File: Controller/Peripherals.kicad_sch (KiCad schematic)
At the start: 3 parts, among them U601 THB001P

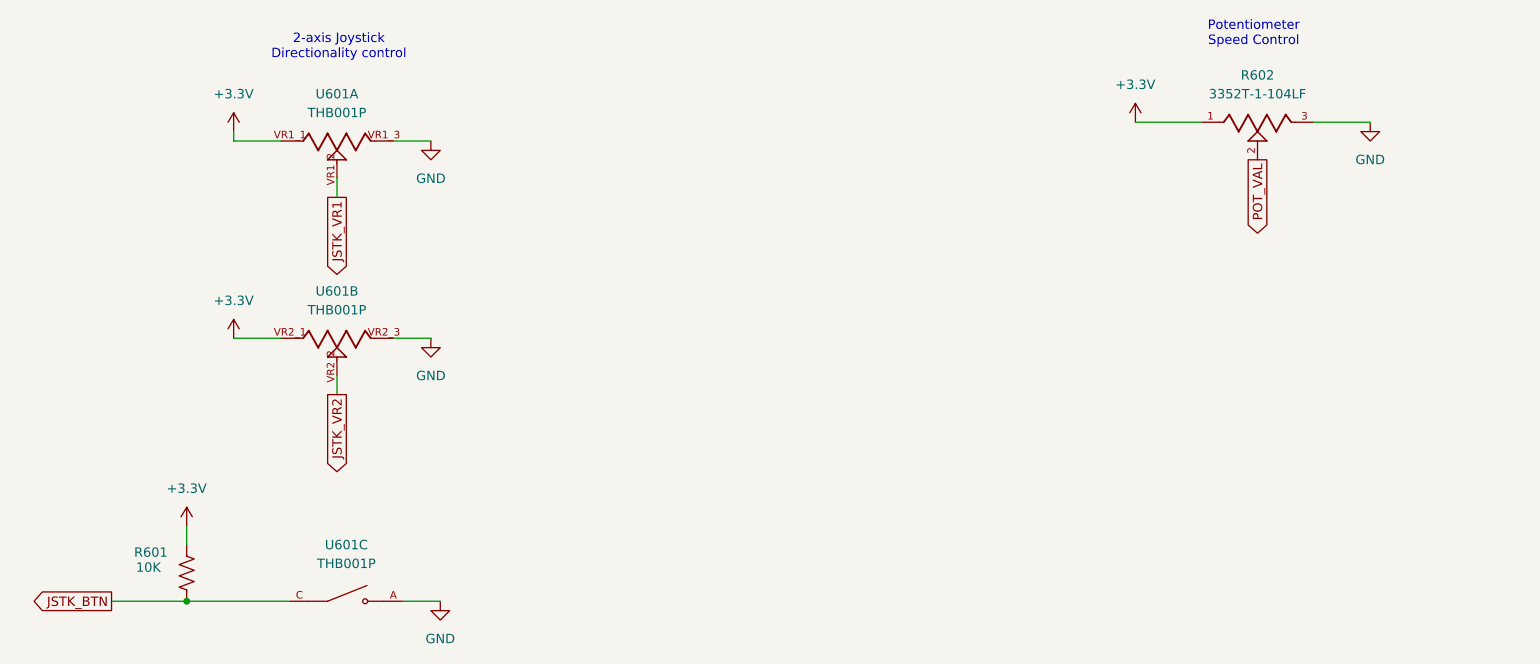
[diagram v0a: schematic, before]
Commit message: Finished layout for controller, ready to order REV 0-1 PCBs
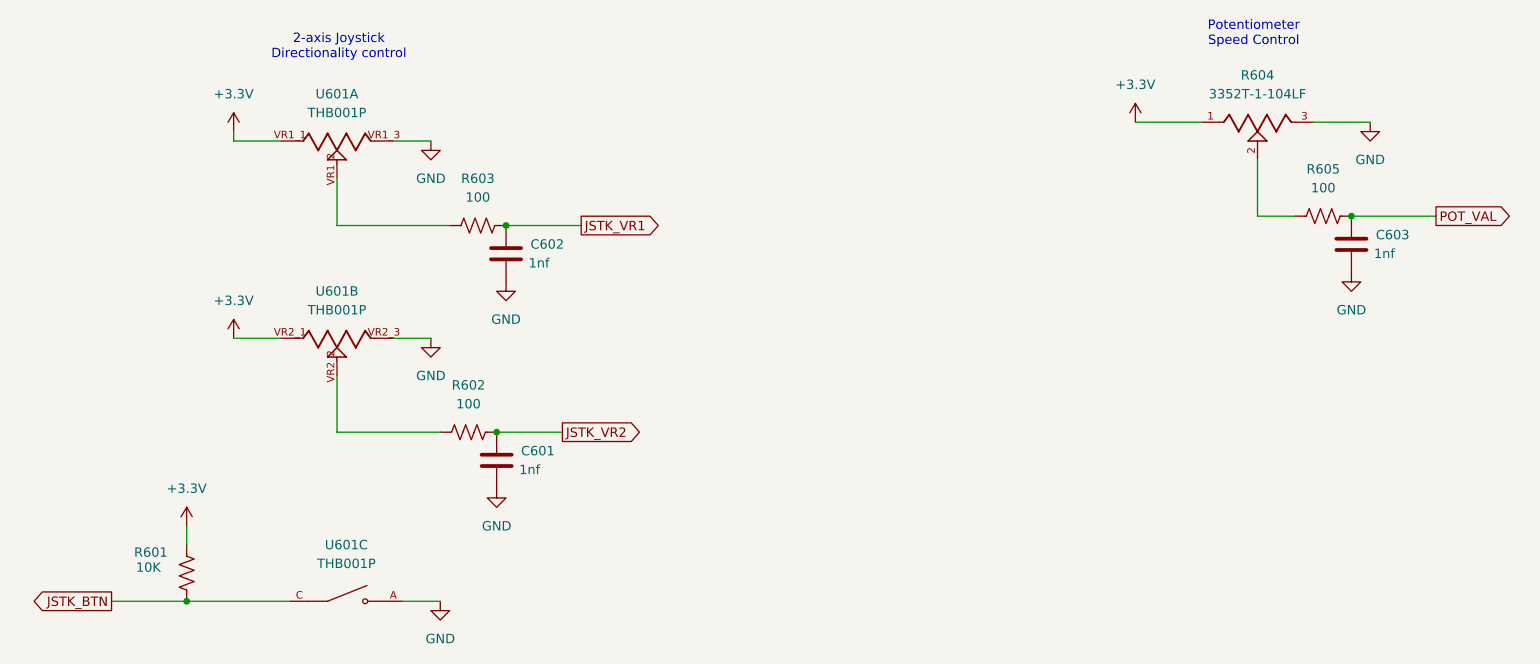
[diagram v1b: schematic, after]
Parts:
- added C601, C602, C603: 1nf, Capacitor_SMD:C_0402_1005Metric, symbol Device:C
- added R602, R603, R605: 100, Resistor_SMD:R_0402_1005Metric, symbol Device:R_US
- renumbered R602 to R604
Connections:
- net GND: now also C601.2, C602.2, C603.2
- net JSTK_VR1: now also C602.1, R603.2; no longer U601.VR1_2
- net JSTK_VR2: now also C601.1, R602.2; no longer U601.VR2_2
- net POT_VAL: now also C603.1, R605.2; no longer R604.2
- new net: R602.1, U601.VR2_2
- new net: R603.1, U601.VR1_2
- new net: R604.2, R605.1

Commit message: Swapped polarity of joystick and speed dial so that values line up correctly with desired control.  In short 3.3V on ADC is max speed rather than no speed.
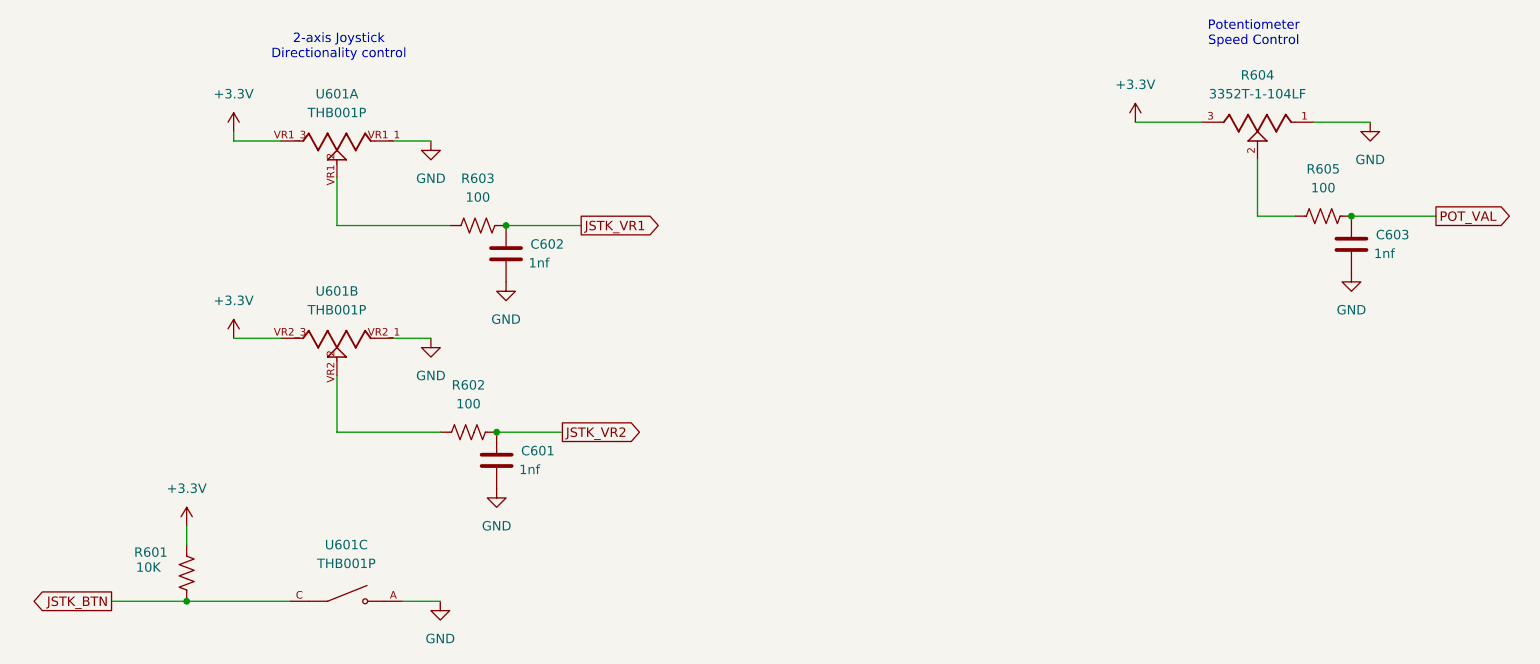
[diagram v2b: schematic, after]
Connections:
- net +3.3V: now also R604.3, U601.VR1_3, U601.VR2_3; no longer R604.1, U601.VR1_1, U601.VR2_1
- net GND: now also R604.1, U601.VR1_1, U601.VR2_1; no longer R604.3, U601.VR1_3, U601.VR2_3
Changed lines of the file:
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@@
+	(wire
+		(pts
+			(xy 91.44 78.74) (xy 96.52 78.74)
+		)
+		(stroke
+			(width 0)
+			(type default)
+		)
+	)
+	(wire
+		(pts
+			(xy 69.85 52.07) (xy 76.2 52.07)
+		)
+		(stroke
+			(width 0)
+			(type default)
+		)
+	)
 	(wire
 		(pts
@@
 	(wire
 		(pts
+			(xy 69.85 78.74) (xy 76.2 78.74)
+		)
+		(stroke
+			(width 0)
+			(type default)
+		)
+	)
+	(wire
+		(pts
 			(xy 63.5 114.3) (xy 77.47 114.3)
 		)
@@
 	(wire
 		(pts
-			(xy 91.44 78.74) (xy 96.52 78.74)
+			(xy 91.44 52.07) (xy 96.52 52.07)
 		)
 		(stroke
@@
 	(wire
 		(pts
-			(xy 69.85 78.74) (xy 76.2 78.74)
-		)
-		(stroke
-			(width 0)
-			(type default)
-		)
-	)
-	(wire
-		(pts
-			(xy 69.85 52.07) (xy 76.2 52.07)
-		)
-		(stroke
-			(width 0)
-			(type default)
-		)
-	)
-	(wire
-		(pts
 			(xy 106.68 63.5) (xy 116.84 63.5)
 		)
@@
 	(wire
 		(pts
-			(xy 91.44 52.07) (xy 96.52 52.07)
+			(xy 53.34 114.3) (xy 63.5 114.3)
 		)
 		(stroke
@@
 		(pts
 			(xy 215.9 49.53) (xy 223.52 49.53)
-		)
-		(stroke
-			(width 0)
-			(type default)
-		)
-	)
-	(wire
-		(pts
-			(xy 53.34 114.3) (xy 63.5 114.3)
 		)
 		(stroke
@@
 		(lib_id "Global:THB001P")
 		(at 83.82 78.74 0)
+		(mirror y)
 		(unit 2)
 		(exclude_from_sim no)
@@
 		(on_board yes)
 		(dnp no)
-		(fields_autoplaced yes)
 		(property "Reference" "U601"
 			(at 83.82 72.39 0)
@@
 		(lib_id "Global:THB001P")
 		(at 83.82 52.07 0)
-		(unit 1)
-		(exclude_from_sim no)
-		(in_bom yes)
-		(on_board yes)
-		(dnp no)
-		(fields_autoplaced yes)
+		(mirror y)
+		(unit 1)
+		(exclude_from_sim no)
+		(in_bom yes)
+		(on_board yes)
+		(dnp no)
 		(property "Reference" "U601"
 			(at 83.82 45.72 0)
@@
 		(lib_id "Global:3352T-1-104LF")
 		(at 208.28 49.53 0)
-		(unit 1)
-		(exclude_from_sim no)
-		(in_bom yes)
-		(on_board yes)
-		(dnp no)
-		(fields_autoplaced yes)
+		(mirror y)
+		(unit 1)
+		(exclude_from_sim no)
+		(in_bom yes)
+		(on_board yes)
+		(dnp no)
 		(property "Reference" "R604"
 			(at 208.28 43.18 0)
